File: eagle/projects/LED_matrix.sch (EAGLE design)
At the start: 141 parts, among them IC1001 7805_T_HORIZONTAL, IC101 4093N, IC102 74LS00, IC103 74193N, IC201 7495N, IC202 74175N, IC301 7495N, IC302 74175N, IC401 7495N, IC402 74175N, IC501 7495N, IC502 74175N, IC901 NE555V, T701 BC548C, T702 BC548C, T703 BC548C, T704 BC548C, T705 BC548C, T706 BC548C, T707 BC548C, T708 BC548C, T709 BC548C, T801 BC548C, T802 BC548C, T803 BC548C, T804 BC548C, T805 BC548C, T806 BC548C, T807 BC548C, T901 BD136, X1001 CLAMP_1X2-T-5MM, X1101 MALE_2X13-T-VERTICAL_2.54MM

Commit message: perpare for release
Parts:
- C101: PART_CODE_BEL (none) -> C_PAC_T_RADIAL_5mm_PITCH_2mm54_VAL_1u
- LED701: FUNCTION (none) -> RND1
- LED702: PURPOSE (none) -> RND2
- LED703: PURPOSE (none) -> RND3
- LED704: PURPOSE (none) -> RND4
- LED705: PURPOSE (none) -> RND5
- LED706: PURPOSE (none) -> RND6
- LED707: PURPOSE (none) -> RND7
- LED708: PURPOSE (none) -> RND8
- LED709: PURPOSE (none) -> RND9
- LED801: PURPOSE (none) -> RND10
- LED802: PURPOSE (none) -> RND11
- LED803: PURPOSE (none) -> RND12
- LED804: PURPOSE (none) -> RND13
- LED805: PURPOSE (none) -> RND14
- LED806: PURPOSE (none) -> RND15
- LED807: PURPOSE (none) -> RND16
- R103: FUNCTION (none) -> REFRESH RATE
- R904: FUNCTION (none) -> BRIGHTNESS
- RPH901: FUNCTION (none) -> LIGHT SENSOR
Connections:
- net N$1 renamed CLK_SLOW_RA
- net N$3 renamed TIM_RA
- net P5V: now also IC102C.I1

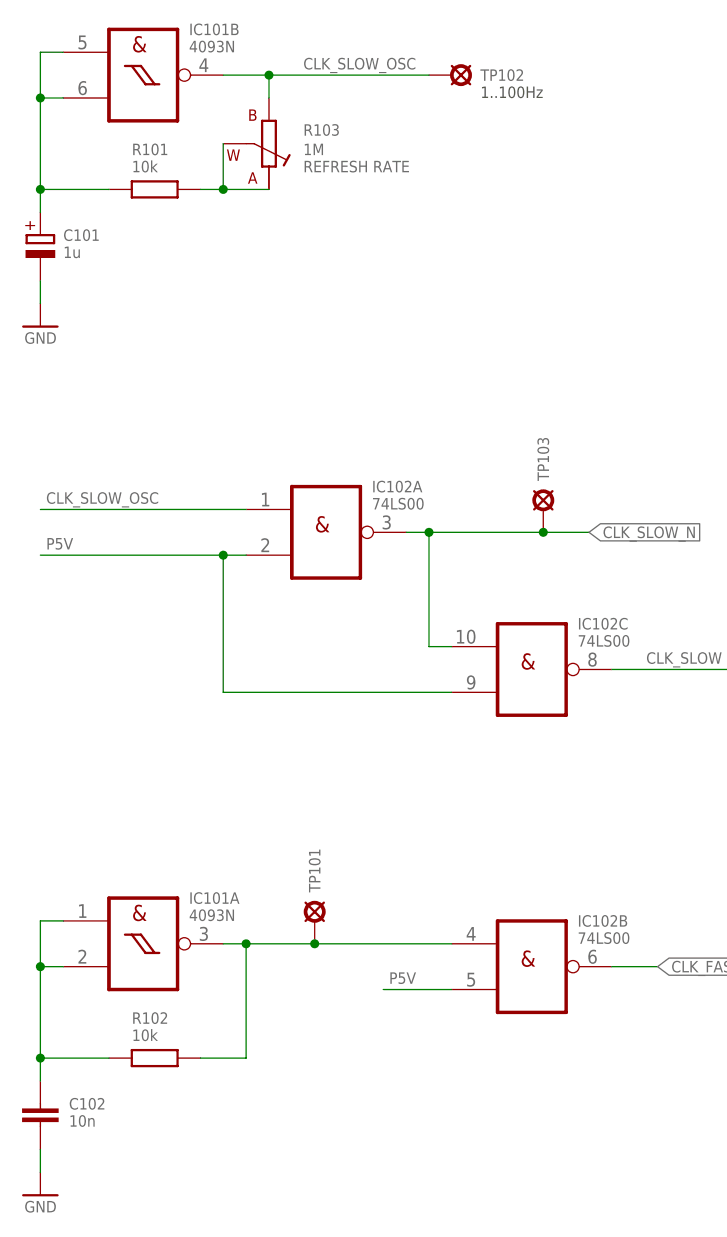
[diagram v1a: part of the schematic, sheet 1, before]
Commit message: changed values for oscillators
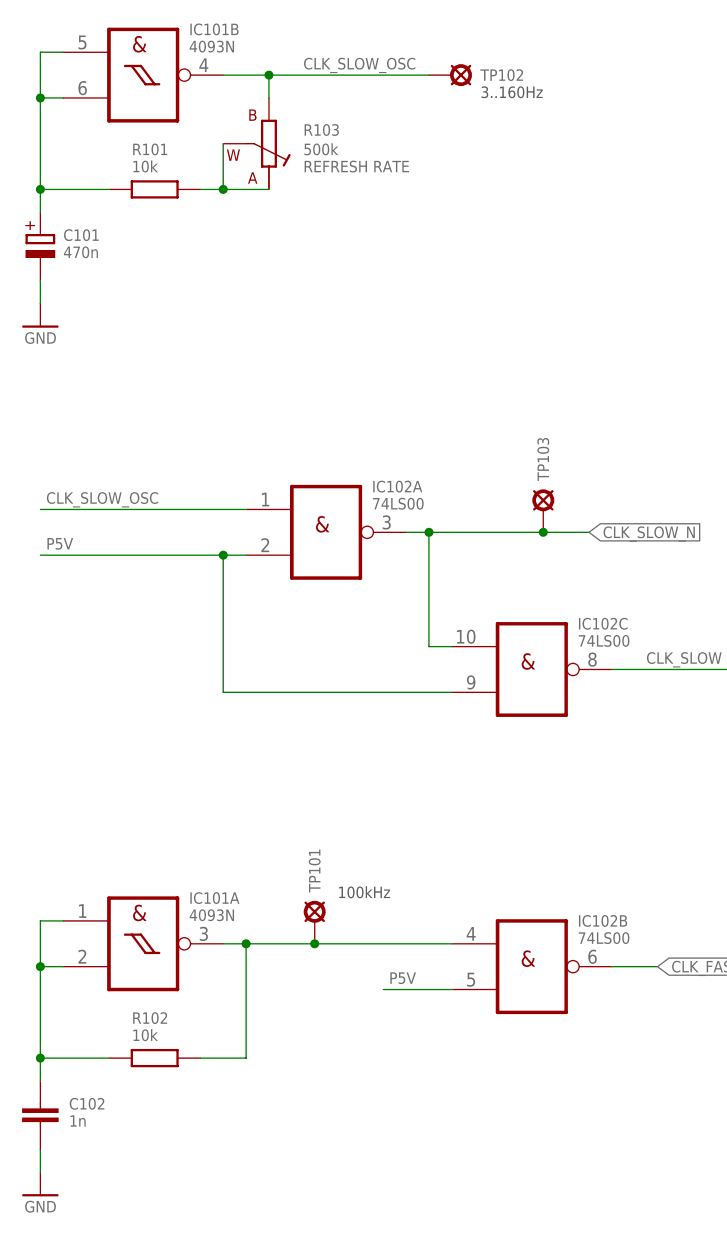
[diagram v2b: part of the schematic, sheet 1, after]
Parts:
- C101: value 1u -> 470n; PART_CODE_BEL C_PAC_T_RADIAL_5mm_PITCH_2mm54_VAL_1u -> C_PAC_T_RADIAL_5mm_PITCH_2mm54_VAL_470n
- C102: value 10n -> 1n
- R103: value 1M -> 500k; PART_CODE_BEL (none) -> R_PAC_T_TRIM_PIHER_PT10_HORIZONTAL_VAL_500k
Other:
- note added: "100kHz"
- note added: "3..160Hz"
- note removed: "1..100Hz"
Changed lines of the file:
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@@
 <part name="FRAME_PRODUCT3" library="be_frame" deviceset="A4_LANDSCAPE_PRODUCT" device=""/>
 <part name="IC101" library="be_logic" deviceset="4093" device="N"/>
-<part name="C102" library="be_rcl" deviceset="C" device="_T_DISC_4MM_PITCH_5MM" value="10n">
+<part name="C102" library="be_rcl" deviceset="C" device="_T_DISC_4MM_PITCH_5MM" value="1n">
 <attribute name="PART_CODE_BEL" value="C_PAC_T_DISC_7mm_PITCH_5mm_VAL_10n"/>
 </part>
@@
 </part>
 <part name="GND1" library="be_supply" deviceset="GND" device=""/>
-<part name="C101" library="be_rcl" deviceset="C_POL" device="_T_RAD5_GRID_2.54" value="1u">
-<attribute name="PART_CODE_BEL" value="C_PAC_T_RADIAL_5mm_PITCH_2mm54_VAL_1u"/>
+<part name="C101" library="be_rcl" deviceset="C_POL" device="_T_RAD5_GRID_2.54" value="470n">
+<attribute name="PART_CODE_BEL" value="C_PAC_T_RADIAL_5mm_PITCH_2mm54_VAL_470n"/>
 </part>
 <part name="R101" library="be_rcl" deviceset="R" device="_T_0207_PITCH_10MM" value="10k">
@@
 <attribute name="PART_CODE_BEL" value="IC_PAC_T_NDIP14_VAL_SN74LS00N"/>
 </part>
-<part name="R103" library="be_rcl" deviceset="RA" device="_T_PT10_HORIZONTAL" value="1M">
+<part name="R103" library="be_rcl" deviceset="RA" device="_T_PT10_HORIZONTAL" value="500k">
 <attribute name="FUNCTION" value="REFRESH RATE"/>
+<attribute name="PART_CODE_BEL" value="R_PAC_T_TRIM_PIHER_PT10_HORIZONTAL_VAL_500k"/>
 </part>
 <part name="TP102" library="be_con_jump" deviceset="TEST_POINT" device="_T_SMALL"/>
@@
 <plain>
 <text x="127" y="142.24" size="1.27" layer="97" font="fixed">count on LH edge</text>
-<text x="64.135" y="152.4" size="1.27" layer="97" font="fixed">1..100Hz</text>
+<text x="64.135" y="152.4" size="1.27" layer="97" font="fixed">3..160Hz</text>
+<text x="48.26" y="63.5" size="1.27" layer="97" font="fixed">100kHz</text>
 </plain>
 <instances>

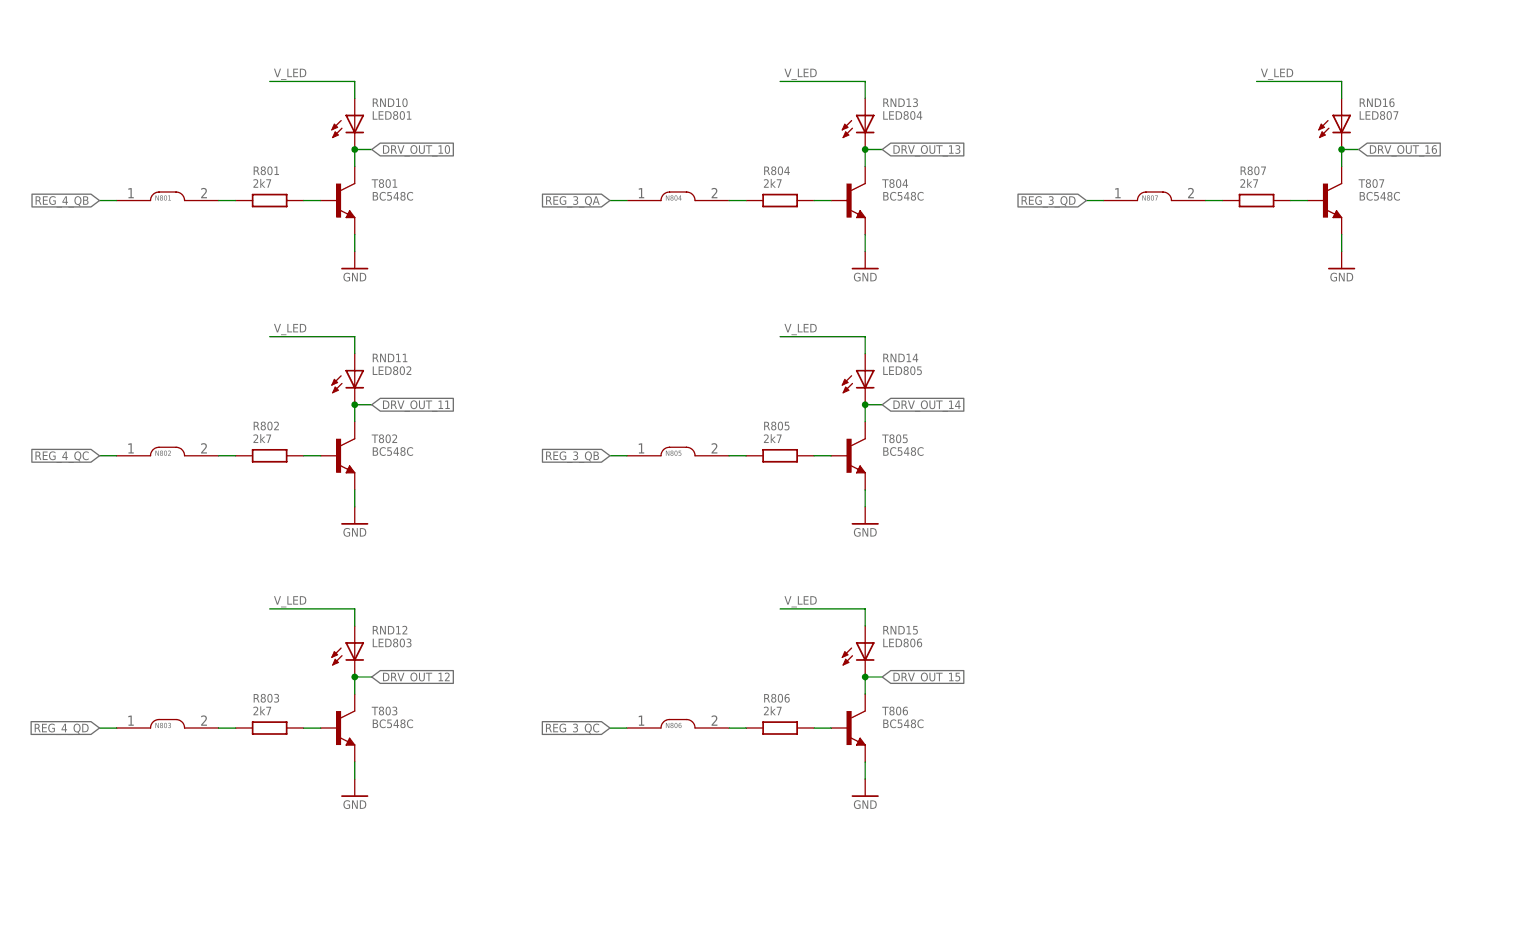
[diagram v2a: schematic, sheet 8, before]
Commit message: add LED resistors
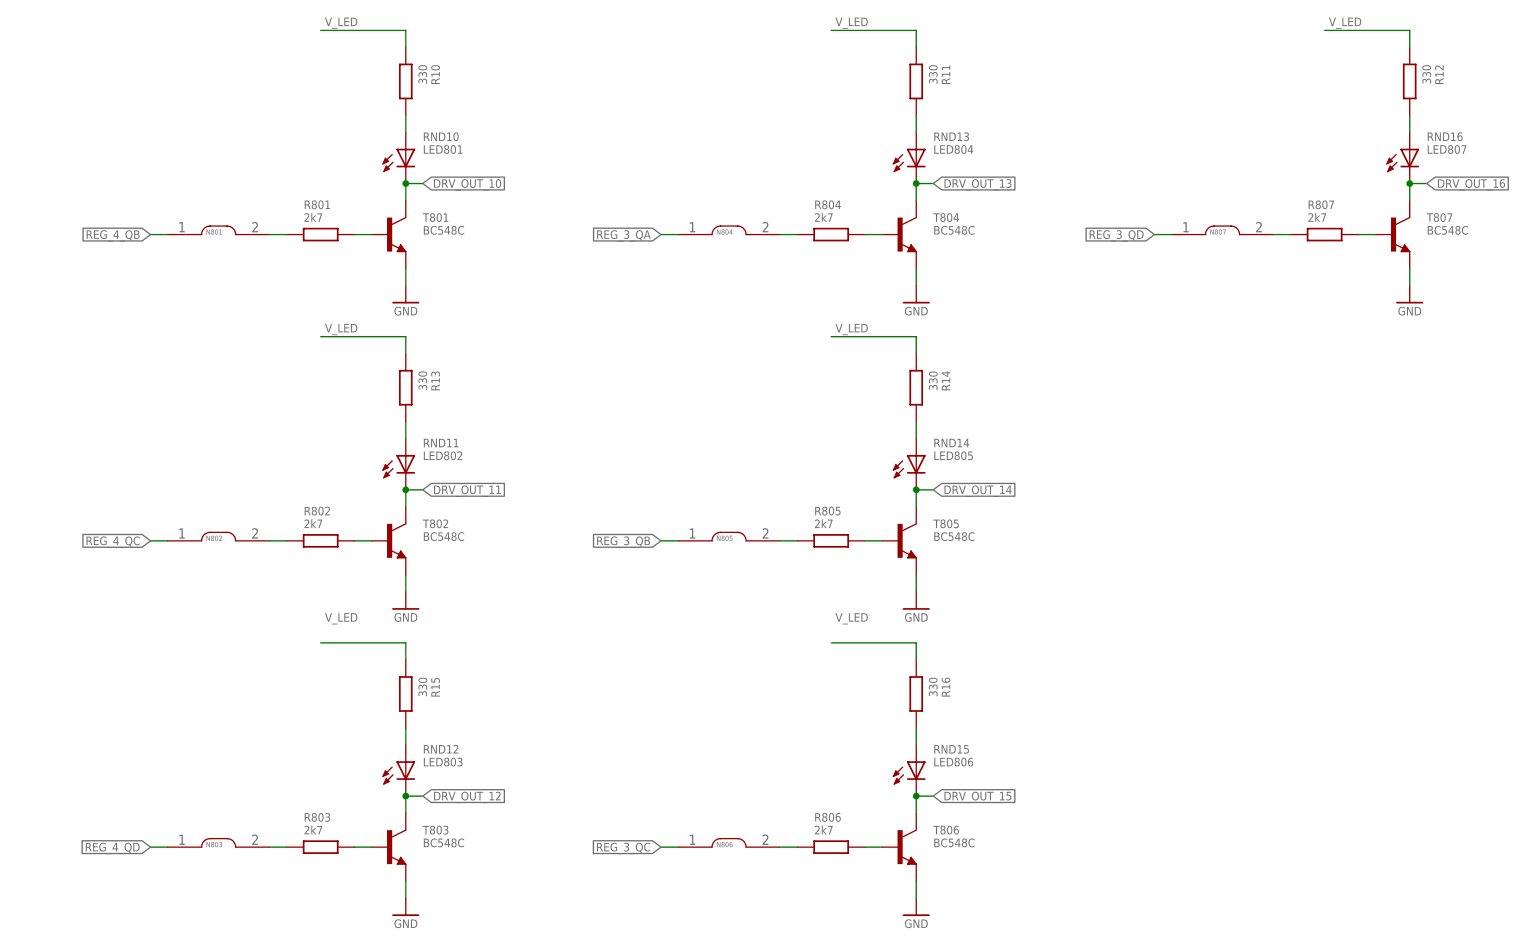
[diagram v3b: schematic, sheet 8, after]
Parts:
- added R1, R10, R11, R12, R13, R14, R15, R16, R2, R3, R4, R5, R6, R7, R8, R9: 330, be_rcl:R_T_0207_PITCH_10MM
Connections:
- new net N$1: LED701.A, R1.2
- new net N$10: LED801.A, R10.2
- new net N$11: LED804.A, R11.2
- new net N$12: LED807.A, R12.2
- new net N$13: LED802.A, R13.2
- new net N$14: LED805.A, R14.2
- new net N$15: LED803.A, R15.2
- new net N$16: LED806.A, R16.2
- new net N$2: LED704.A, R2.2
- new net N$3: LED707.A, R3.2
- new net N$4: LED703.A, R4.2
- new net N$5: LED706.A, R5.2
- new net N$6: LED709.A, R6.2
- new net N$7: LED702.A, R7.2
- new net N$8: LED705.A, R8.2
- new net N$9: LED708.A, R9.2
- net V_LED: now also R1.1, R10.1, R11.1, R12.1, R13.1, R14.1, R15.1, R16.1, R2.1, R3.1, R4.1, R5.1, R6.1, R7.1, R8.1, R9.1; no longer LED701.A, LED702.A, LED703.A, LED704.A, LED705.A, LED706.A, LED707.A, LED708.A, LED709.A, LED801.A, LED802.A, LED803.A, LED804.A, LED805.A, LED806.A, LED807.A
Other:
- moved on the sheet: LED702, LED703, LED705, LED706, LED708, LED709, LED801, LED802, LED803, LED804, LED805, LED806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

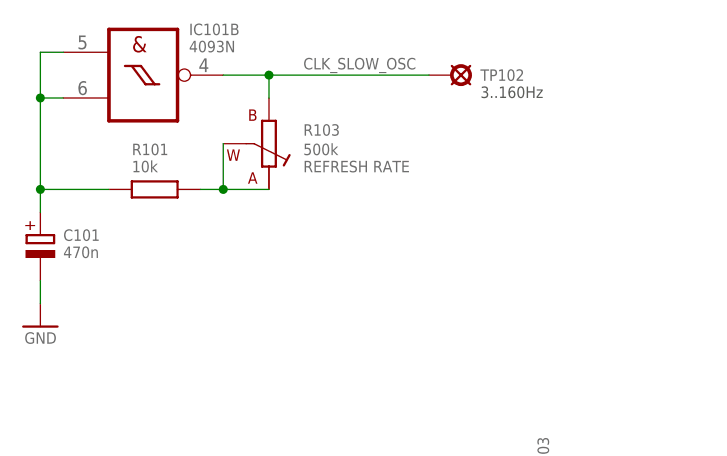
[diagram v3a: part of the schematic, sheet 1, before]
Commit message: rename anonymous nets
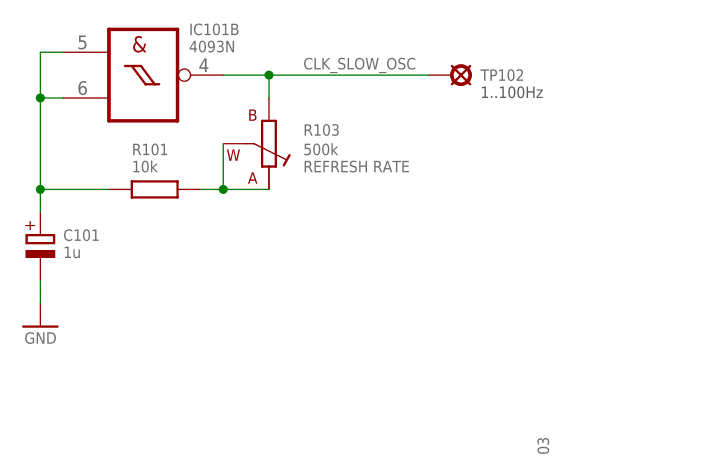
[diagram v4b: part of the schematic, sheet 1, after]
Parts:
- C101: value 470n -> 1u; PART_CODE_BEL C_PAC_T_RADIAL_5mm_PITCH_2mm54_VAL_470n -> C_PAC_T_RADIAL_5mm_PITCH_2mm54_VAL_1u
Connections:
- net N$1 renamed DRV_OUT_A_1
- net N$10 renamed DRV_OUT_A_10
- net N$11 renamed DRV_OUT_A_13
- net N$12 renamed DRV_OUT_A_16
- net N$13 renamed DRV_OUT_A_11
- net N$14 renamed DRV_OUT_A_14
- net N$15 renamed DRV_OUT_A_12
- net N$16 renamed DRV_OUT_A_15
- net N$2 renamed DRV_OUT_A_4
- net N$3 renamed DRV_OUT_A_7
- net N$4 renamed DRV_OUT_A_3
- net N$5 renamed DRV_OUT_A_6
- net N$6 renamed DRV_OUT_A_9
- net N$7 renamed DRV_OUT_A_2
- net N$8 renamed DRV_OUT_A_5
- net N$9 renamed DRV_OUT_A_8
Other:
- note added: "1..100Hz"
- note removed: "3..160Hz"
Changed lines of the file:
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@@
 </part>
 <part name="GND1" library="be_supply" deviceset="GND" device=""/>
-<part name="C101" library="be_rcl" deviceset="C_POL" device="_T_RAD5_GRID_2.54" value="470n">
-<attribute name="PART_CODE_BEL" value="C_PAC_T_RADIAL_5mm_PITCH_2mm54_VAL_470n"/>
+<part name="C101" library="be_rcl" deviceset="C_POL" device="_T_RAD5_GRID_2.54" value="1u">
+<attribute name="PART_CODE_BEL" value="C_PAC_T_RADIAL_5mm_PITCH_2mm54_VAL_1u"/>
 </part>
 <part name="R101" library="be_rcl" deviceset="R" device="_T_0207_PITCH_10MM" value="10k">
@@
 <plain>
 <text x="127" y="142.24" size="1.27" layer="97" font="fixed">count on LH edge</text>
-<text x="64.135" y="152.4" size="1.27" layer="97" font="fixed">3..160Hz</text>
+<text x="64.135" y="152.4" size="1.27" layer="97" font="fixed">1..100Hz</text>
 <text x="48.26" y="63.5" size="1.27" layer="97" font="fixed">100kHz</text>
 </plain>
@@
 </segment>
 </net>
-<net name="N$1" class="0">
+<net name="DRV_OUT_A_1" class="0">
 <segment>
 <pinref part="LED701" gate="G$1" pin="A"/>
@@
 </segment>
 </net>
-<net name="N$2" class="0">
+<net name="DRV_OUT_A_4" class="0">
 <segment>
 <pinref part="R2" gate="G$1" pin="2"/>
@@
 </segment>
 </net>
-<net name="N$3" class="0">
+<net name="DRV_OUT_A_7" class="0">
 <segment>
 <pinref part="R3" gate="G$1" pin="2"/>
@@
 </segment>
 </net>
-<net name="N$4" class="0">
+<net name="DRV_OUT_A_3" class="0">
 <segment>
 <pinref part="R4" gate="G$1" pin="2"/>
@@
 </segment>
 </net>
-<net name="N$5" class="0">
+<net name="DRV_OUT_A_6" class="0">
 <segment>
 <pinref part="R5" gate="G$1" pin="2"/>
@@
 </segment>
 </net>
-<net name="N$6" class="0">
+<net name="DRV_OUT_A_9" class="0">
 <segment>
 <pinref part="R6" gate="G$1" pin="2"/>
@@
 </segment>
 </net>
-<net name="N$7" class="0">
+<net name="DRV_OUT_A_2" class="0">
 <segment>
 <pinref part="R7" gate="G$1" pin="2"/>
@@
 </segment>
 </net>
-<net name="N$8" class="0">
+<net name="DRV_OUT_A_5" class="0">
 <segment>
 <pinref part="R8" gate="G$1" pin="2"/>
@@
 </segment>
 </net>
-<net name="N$9" class="0">
+<net name="DRV_OUT_A_8" class="0">
 <segment>
 <pinref part="R9" gate="G$1" pin="2"/>
@@
 </segment>
 </net>
-<net name="N$10" class="0">
+<net name="DRV_OUT_A_10" class="0">
 <segment>
 <pinref part="R10" gate="G$1" pin="2"/>
@@
 </segment>
 </net>
-<net name="N$11" class="0">
+<net name="DRV_OUT_A_13" class="0">
 <segment>
 <pinref part="R11" gate="G$1" pin="2"/>
@@
 </segment>
 </net>
-<net name="N$12" class="0">
+<net name="DRV_OUT_A_16" class="0">
 <segment>
 <pinref part="R12" gate="G$1" pin="2"/>
@@
 </segment>
 </net>
-<net name="N$13" class="0">
+<net name="DRV_OUT_A_11" class="0">
 <segment>
 <pinref part="R13" gate="G$1" pin="2"/>
@@
 </segment>
 </net>
-<net name="N$14" class="0">
+<net name="DRV_OUT_A_14" class="0">
 <segment>
 <pinref part="R14" gate="G$1" pin="2"/>
@@
 </segment>
 </net>
-<net name="N$15" class="0">
+<net name="DRV_OUT_A_12" class="0">
 <segment>
 <pinref part="R15" gate="G$1" pin="2"/>
@@
 </segment>
 </net>
-<net name="N$16" class="0">
+<net name="DRV_OUT_A_15" class="0">
 <segment>
 <pinref part="R16" gate="G$1" pin="2"/>

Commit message: release
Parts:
- removed R1, R10, R13, R15, R4, R7: 330, be_rcl:R_T_0207_PITCH_10MM
- added R713, R714, R715, R808, R809, R813: 2k7, be_rcl:R_T_0207_PITCH_10MM
- R704, R705, R706, R804, R805, R806: value 2k7 -> 330; PART_CODE_BEL (none) -> R_PAC_T_0207_PITCH_10mm_VAL_330
- X1101: value MALE_2X13-T-VERTICAL_2.54MM -> MALE_2X13-T-VERTICAL_PITCH_2MM54; device be_con_jump:MALE_2X13-T-VERTICAL_2.54MM -> be_con_jump:MALE_2X13-T-VERTICAL_PITCH_2MM54
- renumbered R11 to R810, R12 to R814, R14 to R811, R16 to R812, R2 to R710, R3 to R716, R5 to R712, R6 to R718, R8 to R711, R9 to R717
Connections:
- net DRV_IN_13: now also R807.1; no longer R804.1
- net DRV_IN_14: now also R808.1; no longer R805.1
- net DRV_IN_15: now also R809.1; no longer R806.1
- net DRV_IN_16: now also R813.1; no longer R807.1
- net DRV_IN_4: now also R707.1; no longer R704.1
- net DRV_IN_5: now also R708.1; no longer R705.1
- net DRV_IN_6: now also R709.1; no longer R706.1
- net DRV_IN_7: now also R713.1; no longer R707.1
- net DRV_IN_8: now also R714.1; no longer R708.1
- net DRV_IN_9: now also R715.1; no longer R709.1
- net DRV_IN_B13: now also R807.2; no longer R804.2
- net DRV_IN_B14: now also R808.2; no longer R805.2
- net DRV_IN_B15: now also R809.2; no longer R806.2
- net DRV_IN_B16: now also R813.2; no longer R807.2
- net DRV_IN_B4: now also R707.2; no longer R704.2
- net DRV_IN_B5: now also R708.2; no longer R705.2
- net DRV_IN_B6: now also R709.2; no longer R706.2
- net DRV_IN_B7: now also R713.2; no longer R707.2
- net DRV_IN_B8: now also R714.2; no longer R708.2
- net DRV_IN_B9: now also R715.2; no longer R709.2
- net DRV_OUT_A_1: now also R704.2; no longer R1.2
- net DRV_OUT_A_10: now also R804.2; no longer R10.2
- net DRV_OUT_A_11: now also R805.2; no longer R13.2
- net DRV_OUT_A_12: now also R806.2; no longer R15.2
- net DRV_OUT_A_2: now also R705.2; no longer R7.2
- net DRV_OUT_A_3: now also R706.2; no longer R4.2
- net V_LED: now also R704.1, R705.1, R706.1, R804.1, R805.1, R806.1; no longer R1.1, R10.1, R13.1, R15.1, R4.1, R7.1
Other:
- moved on the sheet: R704, R705, R706, R707, R708, R709, R804, R805, R806, R807

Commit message: fix values. add movie
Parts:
- C102: value 1n -> 100n; PART_CODE_BEL C_PAC_T_DISC_7mm_PITCH_5mm_VAL_10n -> C_PAC_T_DISC_7mm_PITCH_5mm_VAL_100n
- R103: value 500k -> 50k; PART_CODE_BEL R_PAC_T_TRIM_PIHER_PT10_HORIZONTAL_VAL_500k -> R_PAC_T_TRIM_PIHER_PT10_HORIZONTAL_VAL_50k
- R901: value 10k -> 1k2
- R902: value 470k -> not fitted
- R905: value 1k -> 10k; PART_CODE_BEL R_PAC_S_0805_VAL_1k -> R_PAC_S_0805_VAL_10k
- R906: value 1k -> 330; PART_CODE_BEL R_PAC_S_0805_VAL_1k -> R_PAC_S_0805_VAL_330
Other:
- note added: "1kHz"
- note added: "20..100Hz"
- note added: "dark: 200Hz bright: 10kHz 50us fixed low time"
- note removed: "1..100Hz"
- note removed: "100kHz"
